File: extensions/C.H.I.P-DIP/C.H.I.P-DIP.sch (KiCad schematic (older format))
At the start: 1 part, among them U1 C.H.I.P

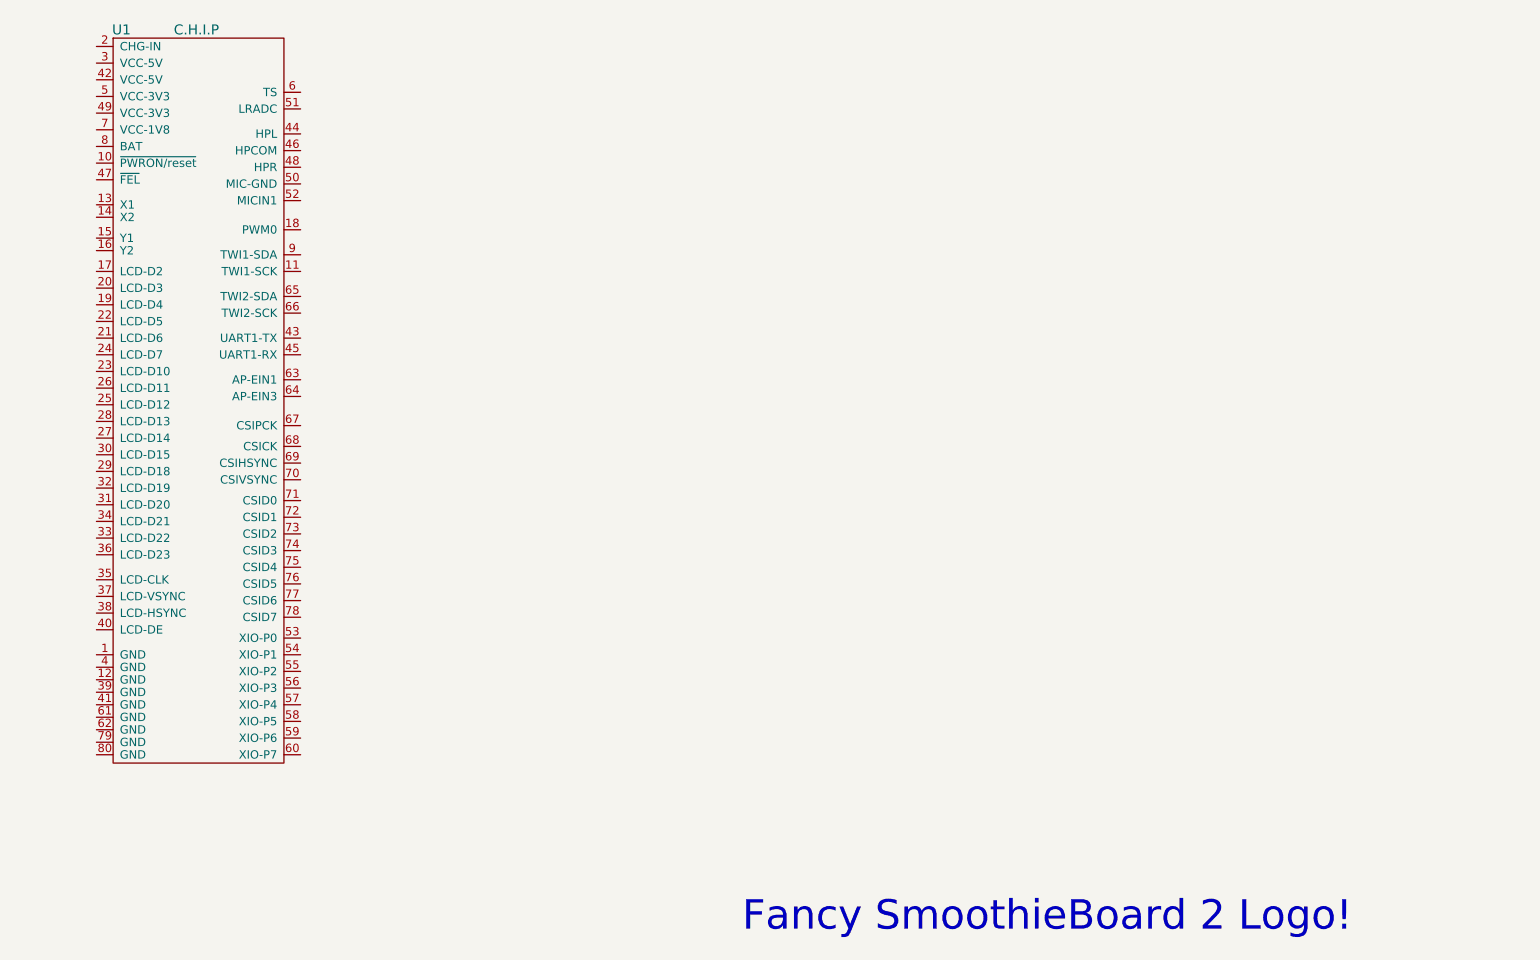
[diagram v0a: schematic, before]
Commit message: Added C.H.I.P expander board
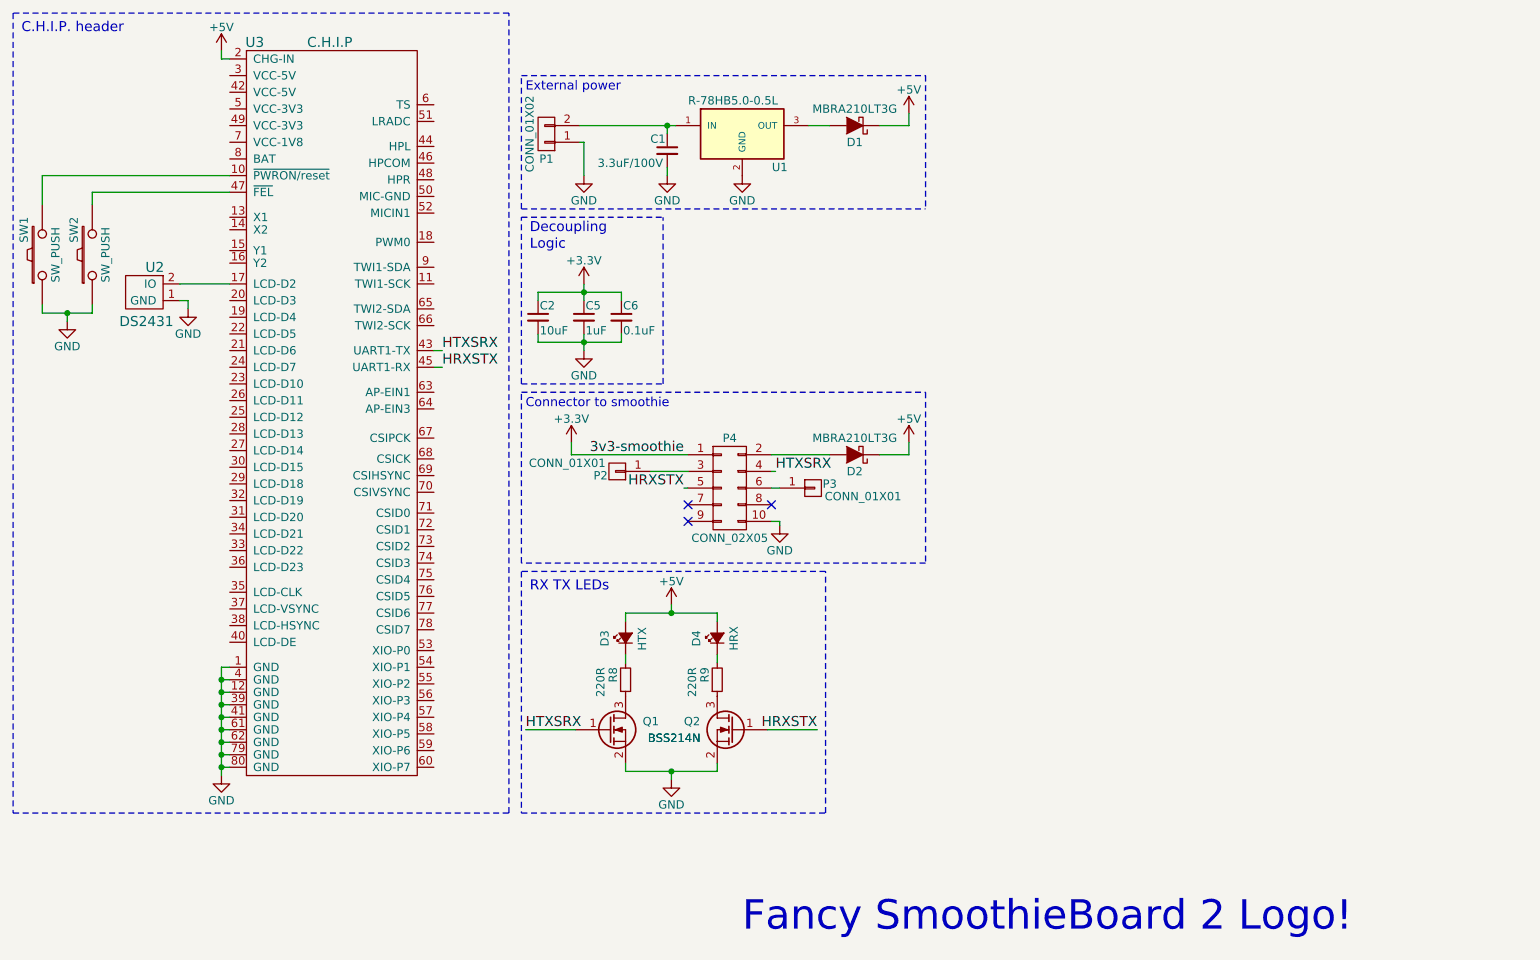
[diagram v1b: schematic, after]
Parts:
- removed U1: C.H.I.P, C.H.I.P:C.H.I.P, symbol C.H.I.P
- added C1: 3.3uF/100V, Capacitors_SMD:C_1206, symbol C_Small
- added C2: 10uF, Capacitors_SMD:C_0603, symbol C_Small
- added C5: 1uF, Capacitors_SMD:C_0603, symbol C_Small
- added C6: 0.1uF, Capacitors_SMD:C_0603, symbol C_Small
- added D1, D2: MBRA210LT3G, Diodes_SMD:D_SMA_Standard, symbol D_Schottky
- added D3: HTX, Diodes_SMD:D_0805, symbol Led_Small
- added D4: HRX, Diodes_SMD:D_0805, symbol Led_Small
- added P1: CONN_01X02, Smoothie-Connectors:FCI_20020110-C021A01LF, symbol CONN_01X02
- added P2, P3: CONN_01X01, Pin_Headers:Pin_Header_Straight_1x01_Pitch2.54mm, symbol CONN_01X01
- added P4: CONN_02X05, Smoothie-Connectors:SHF-105-01-L-D-SM-LC, symbol CONN_02X05
- added Q1, Q2: BSS214N, TO_SOT_Packages_SMD:SOT-23, symbol Q_NMOS_GSD
- added R8, R9: 220R, Resistors_SMD:R_0603, symbol R_Small
- added SW1, SW2: SW_PUSH, Buttons_Switches_SMD:SW_SPST_EVPBF, symbol SW_PUSH
- added U1: R-78HB5.0-0.5L, Smoothie-Regulators:R-78HBx.x-x.xL, symbol LM7805CT
- added U2: DS2431, Smoothie-TSOC:TSOC-6, symbol DS2431
- added U3: C.H.I.P, C.H.I.P:C.H.I.P, symbol C.H.I.P
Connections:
- new net: D2.2 (A), P4.2 (P2)
- new net: P2.1 (P1), P4.3 (P3)
- new net: P3.1 (P1), P4.6 (P6)
- new net: C1.1, P1.2 (P2), U1.1 (IN)
- new net: D1.2 (A), U1.3 (OUT)
- new net: D3.1 (K), R8.2
- new net: D4.1 (K), R9.2
- new net: Q1.3 (D), R8.1
- new net: Q2.3 (D), R9.1
- new net: SW1.2, U3.10 (~PWRON/reset)
- new net: U2.2 (IO), U3.17 (LCD-D2)
- new net: SW2.2, U3.47 (~FEL)
- new net +3V3: C2.1, C5.1, C6.1, P4.1 (P1)
- new net +5V: D1.1 (K), D2.1 (K), D3.2 (A), D4.2 (A), U3.2 (CHG-IN)
- new net GND: C1.2, C2.2, C5.2, C6.2, P1.1 (P1), P4.10 (P10), Q1.2 (S), Q2.2 (S), SW1.1, SW2.1, U1.2 (GND), U2.1 (GND), U3.1 (GND), U3.12 (GND), U3.39 (GND), U3.4 (GND), U3.41 (GND), U3.61 (GND), U3.62 (GND), U3.79 (GND), U3.80 (GND)
- new net HRXSTX: P4.5 (P5), Q2.1 (G), U3.45 (UART1-RX)
- new net HTXSRX: P4.4 (P4), Q1.1 (G), U3.43 (UART1-TX)
- no-connect marks 0 -> 3
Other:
- note added: "C.H.I.P. header"
- note added: "Connector to smoothie"
- note added: "Decoupling"
- note added: "External power"
- note added: "Logic"
- note added: "RX TX LEDs"
